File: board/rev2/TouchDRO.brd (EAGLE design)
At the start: 50.8 x 50.8 mm, 26 parts, among them U2 VREG_33, U3 VREG_5

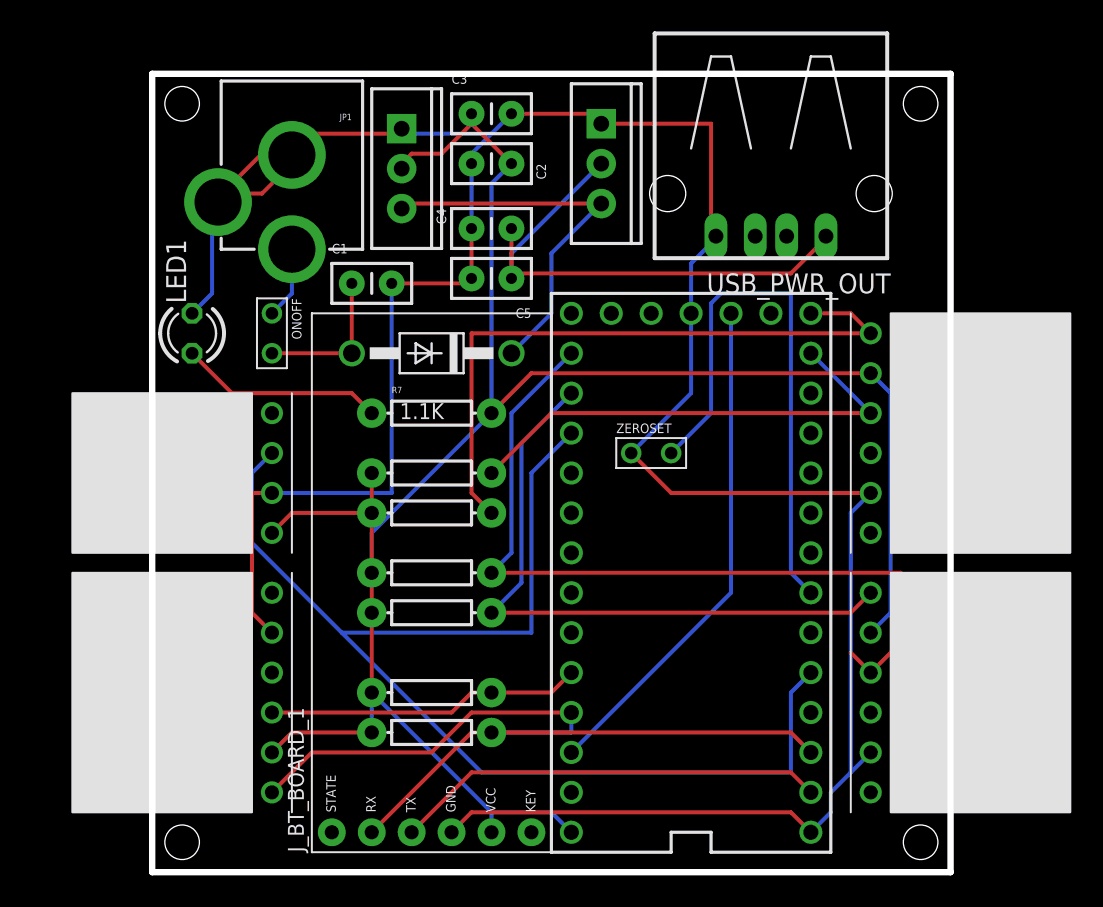
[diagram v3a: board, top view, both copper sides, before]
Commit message: move zero set connection point into reasonable location
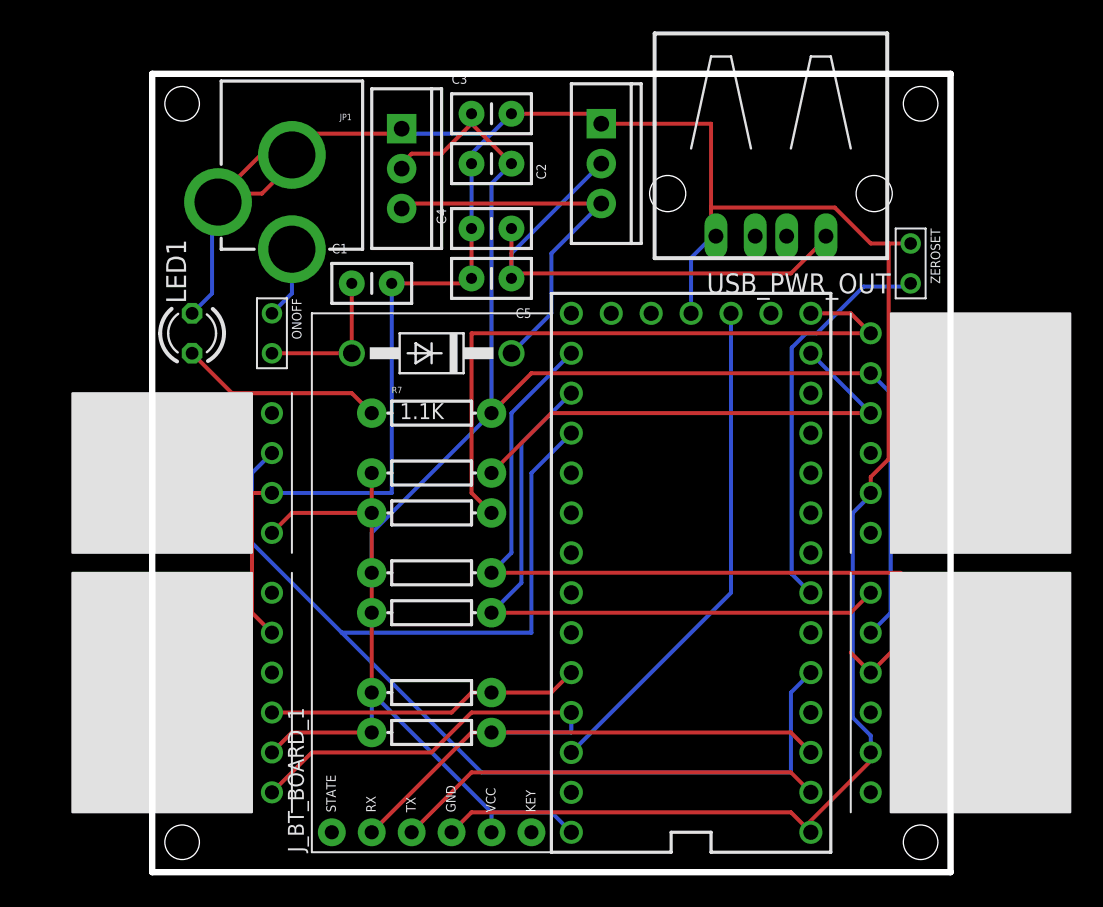
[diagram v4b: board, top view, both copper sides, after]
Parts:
- moved ZEROSET 18.7 mm to (48.3, 37.5), turned to 270 degrees
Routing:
- net ZSET: track 35.5 -> 25.5 mm
- net GND: track 183.8 -> 186.6 mm
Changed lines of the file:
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@@
 <element name="R5" library="SparkFun-Passives" package="AXIAL-0.3EZ" value="10K" x="17.78" y="11.43" smashed="yes"/>
 <element name="R6" library="SparkFun-Passives" package="AXIAL-0.3EZ" value="10K" x="17.78" y="8.89" smashed="yes"/>
-<element name="ZEROSET" library="Switches" package="DS-EXT" value="DS-227" x="33.02" y="26.67"/>
+<element name="ZEROSET" library="Switches" package="DS-EXT" value="DS-227" x="48.26" y="37.465" rot="R270"/>
 <element name="ONOFF" library="Switches" package="DS-EXT" value="DS-228" x="7.62" y="33.02" rot="R270"/>
 <element name="U2" library="regulators" package="TO220" value="VREG_33" x="15.875" y="44.7675" rot="R270"/>
@@
 <contactref element="LED1" pad="K"/>
 <contactref element="USB_PWR_OUT" pad="4"/>
-<wire x1="43.18" y1="5.08" x2="44.45" y2="6.35" width="0.254" layer="16"/>
-<wire x1="44.45" y1="6.35" x2="45.72" y2="7.62" width="0.254" layer="16"/>
-<wire x1="43.18" y1="3.81" x2="43.18" y2="5.08" width="0.254" layer="16"/>
-<wire x1="41.91" y1="2.54" x2="43.18" y2="3.81" width="0.254" layer="16"/>
-<wire x1="44.45" y1="22.86" x2="45.72" y2="24.13" width="0.254" layer="16"/>
-<wire x1="44.45" y1="6.35" x2="44.45" y2="22.86" width="0.254" layer="16"/>
 <wire x1="20.32" y1="3.81" x2="19.05" y2="2.54" width="0.254" layer="1"/>
 <wire x1="40.64" y1="3.81" x2="20.32" y2="3.81" width="0.254" layer="1"/>
@@
 <contactref element="C3" pad="2"/>
 <contactref element="C5" pad="2"/>
-<wire x1="34.29" y1="30.48" x2="30.48" y2="26.67" width="0.254" layer="16"/>
-<wire x1="34.29" y1="35.56" x2="34.29" y2="30.48" width="0.254" layer="16"/>
-<wire x1="34.29" y1="38.735" x2="35.56" y2="40.005" width="0.254" layer="16"/>
-<wire x1="34.29" y1="35.56" x2="34.29" y2="38.735" width="0.254" layer="16"/>
-<wire x1="35.56" y1="40.005" x2="35.87" y2="40.47" width="0.254" layer="16"/>
 <wire x1="6.985" y1="43.18" x2="8.89" y2="45.085" width="0.254" layer="1"/>
 <wire x1="4.445" y1="43.18" x2="6.985" y2="43.18" width="0.254" layer="1"/>
@@
 <wire x1="4.445" y1="43.18" x2="4.19" y2="42.64" width="0.254" layer="1"/>
 <wire x1="15.875" y1="46.99" x2="15.875" y2="47.3075" width="0.254" layer="1"/>
-<wire x1="35.56" y1="47.625" x2="35.56" y2="40.64" width="0.254" layer="1"/>
+<wire x1="35.56" y1="47.625" x2="35.56" y2="42.291" width="0.254" layer="1"/>
+<wire x1="35.56" y1="42.291" x2="35.56" y2="40.64" width="0.254" layer="1"/>
 <wire x1="28.575" y1="47.625" x2="35.56" y2="47.625" width="0.254" layer="1"/>
 <wire x1="35.56" y1="40.64" x2="35.87" y2="40.47" width="0.254" layer="1"/>
@@
 <wire x1="3.81" y1="42.545" x2="3.81" y2="36.83" width="0.254" layer="16"/>
 <wire x1="3.81" y1="42.545" x2="4.19" y2="42.64" width="0.254" layer="16"/>
-<wire x1="33.02" y1="24.13" x2="30.48" y2="26.67" width="0.254" layer="1"/>
-<wire x1="45.72" y1="24.13" x2="33.02" y2="24.13" width="0.254" layer="1"/>
 <wire x1="15.24" y1="24.13" x2="7.62" y2="24.13" width="0.254" layer="16"/>
 <wire x1="15.24" y1="37.465" x2="15.24" y2="24.13" width="0.254" layer="16"/>
+<wire x1="45.72" y1="7.0866" x2="45.72" y2="7.62" width="0.254" layer="1"/>
+<wire x1="41.6052" y1="2.9718" x2="45.72" y2="7.0866" width="0.254" layer="1"/>
+<wire x1="41.6052" y1="2.9718" x2="41.91" y2="2.54" width="0.254" layer="1"/>
+<wire x1="45.72" y1="40.005" x2="46.863" y2="40.005" width="0.254" layer="1"/>
+<wire x1="46.863" y1="40.005" x2="48.26" y2="40.005" width="0.254" layer="1"/>
+<wire x1="43.434" y1="42.291" x2="45.72" y2="40.005" width="0.254" layer="1"/>
+<wire x1="35.56" y1="42.291" x2="43.434" y2="42.291" width="0.254" layer="1"/>
+<wire x1="45.72" y1="25.146" x2="45.72" y2="24.13" width="0.254" layer="1"/>
+<wire x1="46.863" y1="26.289" x2="45.72" y2="25.146" width="0.254" layer="1"/>
+<wire x1="46.863" y1="40.005" x2="46.863" y2="26.289" width="0.254" layer="1"/>
+<wire x1="34.29" y1="39.0906" x2="34.29" y2="35.56" width="0.254" layer="16"/>
+<wire x1="35.6616" y1="40.4622" x2="34.29" y2="39.0906" width="0.254" layer="16"/>
+<wire x1="35.6616" y1="40.4622" x2="35.87" y2="40.47" width="0.254" layer="16"/>
+<wire x1="45.72" y1="8.6868" x2="45.72" y2="7.62" width="0.254" layer="16"/>
+<wire x1="44.577" y1="9.8298" x2="45.72" y2="8.6868" width="0.254" layer="16"/>
+<wire x1="44.577" y1="22.86" x2="44.577" y2="9.8298" width="0.254" layer="16"/>
+<wire x1="45.72" y1="24.003" x2="44.577" y2="22.86" width="0.254" layer="16"/>
+<wire x1="45.72" y1="24.003" x2="45.72" y2="24.13" width="0.254" layer="16"/>
 </signal>
 <signal name="RCV">
@@
 <contactref element="U$1" pad="5"/>
 <contactref element="ZEROSET" pad="P$2"/>
-<wire x1="35.56" y1="29.21" x2="33.02" y2="26.67" width="0.254" layer="16"/>
-<wire x1="35.56" y1="36.195" x2="35.56" y2="29.21" width="0.254" layer="16"/>
-<wire x1="36.195" y1="36.83" x2="35.56" y2="36.195" width="0.254" layer="16"/>
-<wire x1="40.64" y1="36.83" x2="36.195" y2="36.83" width="0.254" layer="16"/>
-<wire x1="40.64" y1="19.05" x2="40.64" y2="36.83" width="0.254" layer="16"/>
-<wire x1="41.91" y1="17.78" x2="40.64" y2="19.05" width="0.254" layer="16"/>
+<wire x1="45.2628" y1="37.2618" x2="48.2346" y2="37.2618" width="0.254" layer="16"/>
+<wire x1="42.291" y1="34.29" x2="45.2628" y2="37.2618" width="0.254" layer="16"/>
+<wire x1="41.6052" y1="34.29" x2="42.291" y2="34.29" width="0.254" layer="16"/>
+<wire x1="40.6908" y1="33.3756" x2="41.6052" y2="34.29" width="0.254" layer="16"/>
+<wire x1="40.6908" y1="18.9738" x2="40.6908" y2="33.3756" width="0.254" layer="16"/>
+<wire x1="41.8338" y1="17.8308" x2="40.6908" y2="18.9738" width="0.254" layer="16"/>
+<wire x1="48.2346" y1="37.2618" x2="48.26" y2="37.465" width="0.254" layer="16"/>
+<wire x1="41.8338" y1="17.8308" x2="41.91" y2="17.78" width="0.254" layer="16"/>
 </signal>
 <signal name="N$1">

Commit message: added bluetooth KEY signal. changed pins in microcontroller code to match new design
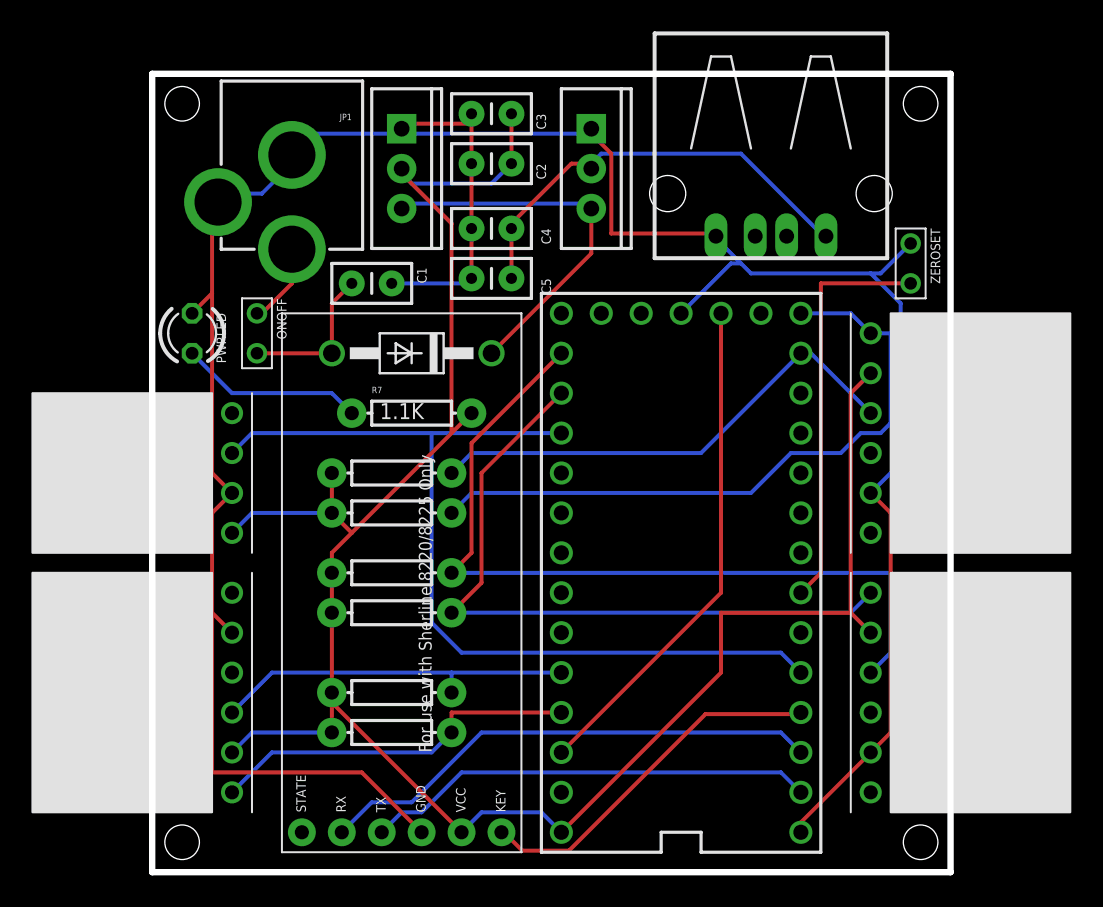
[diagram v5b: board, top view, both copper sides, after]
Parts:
- moved R1 2.54 mm to (15.2, 25.4)
- moved R2 2.54 mm to (15.2, 22.9)
- moved R3 2.54 mm to (15.2, 19.1)
- moved R4 2.54 mm to (15.2, 16.5)
- moved R5 2.54 mm to (15.2, 11.4)
- moved R6 2.54 mm to (15.2, 8.89)
- moved TACH 2.54 mm to (5.08, 21.6)
- moved Z_AXIS 2.54 mm to (-1.27, 8.89)
- moved C3 2.54 mm to (22.9, 48.3), turned to 180 degrees
- moved J_BT_BOARD_1 1.91 mm to (15.9, 19.1)
- moved D3 1.27 mm to (16.5, 33.0)
- moved R7 1.27 mm to (16.5, 29.2)
- moved ONOFF 0.95 mm to (6.67, 33.0)
- moved U3 0.71 mm to (27.9, 44.8)
- moved U$1 0.63 mm to (33.7, 19.1)
- renumbered LED1 to PWRLED
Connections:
- new net KEY: J_BT_BOARD_1.KEY, U$1.2
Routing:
- net KEY: track 0.00 -> 23.2 mm
- net T: track 79.3 -> 58.4 mm
- net GND: track 186.6 -> 176.7 mm
- net +5V: track 33.9 -> 28.1 mm
- net +3V3: track 130.4 -> 134.6 mm
- net Z_B: track 27.5 -> 23.8 mm
- net Y_B: track 40.7 -> 44.1 mm
- net Z_A: track 20.1 -> 23.3 mm
- net RCV: track 27.5 -> 28.8 mm
- net N$1: track 13.0 -> 11.7 mm
- net TR: track 31.1 -> 32.4 mm
- net Y_A: track 51.0 -> 51.7 mm
- net N$6: track 4.61 -> 5.19 mm
- net X_B: track 41.7 -> 42.3 mm

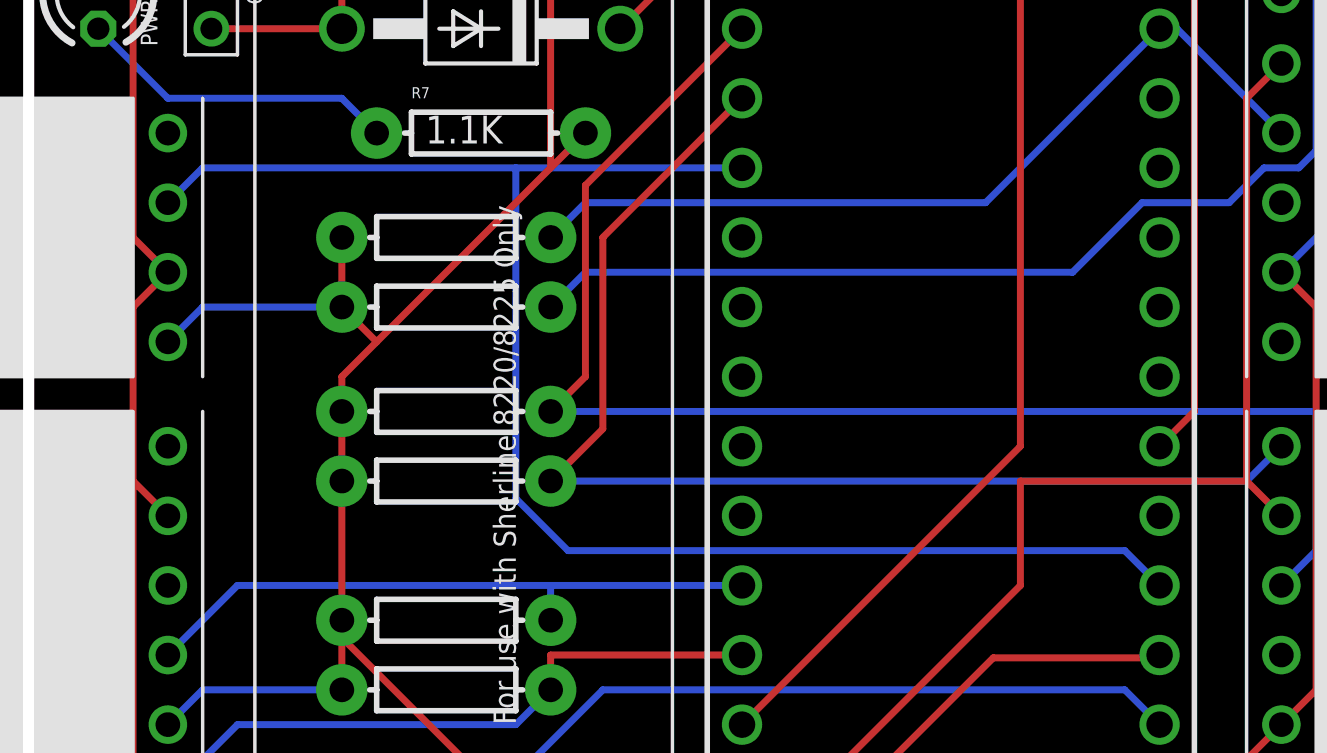
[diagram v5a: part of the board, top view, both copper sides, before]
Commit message: modified rev2 board to use multifrequencymeasure library (which allows to specify of pin)
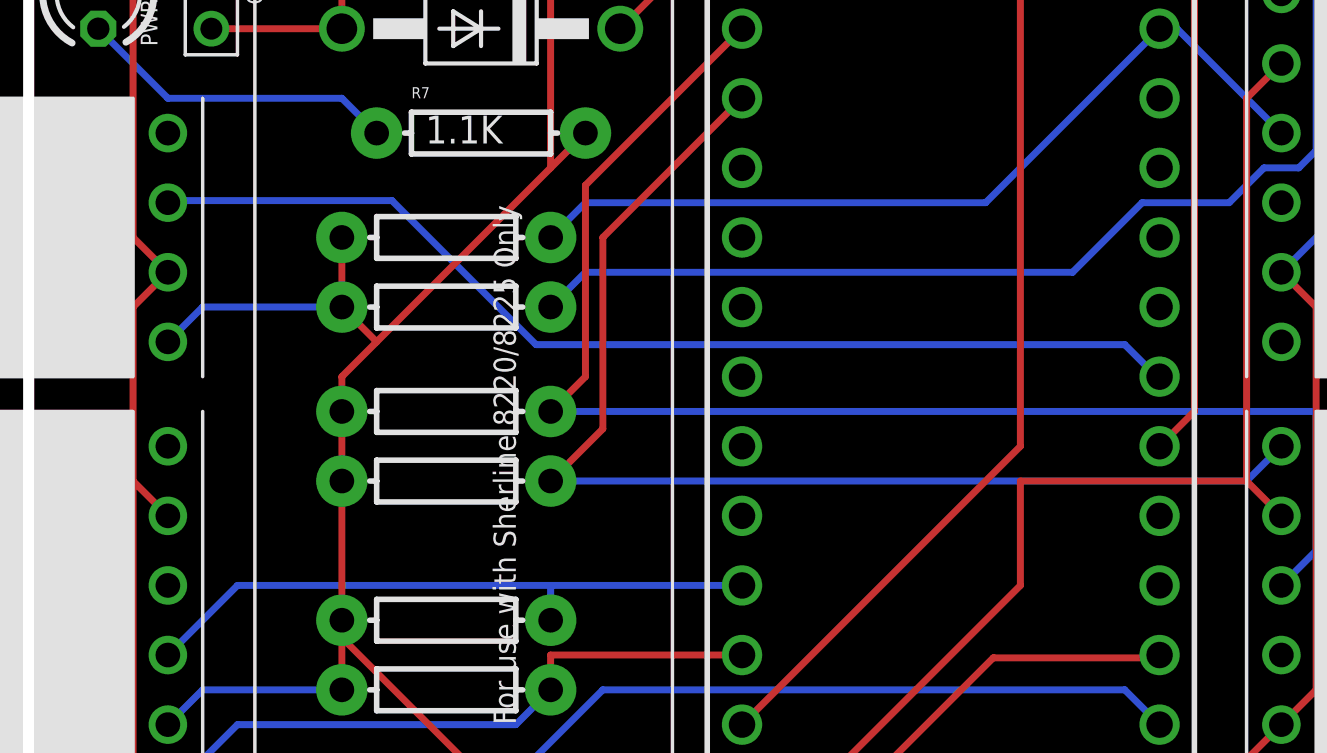
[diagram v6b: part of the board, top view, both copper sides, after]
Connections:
- net T: now also U$1.6; no longer U$1.16/A2, U$1.3
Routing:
- net T: track 58.4 -> 38.9 mm
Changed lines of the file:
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@@
 <signal name="T">
 <contactref element="TACH" pad="P$3"/>
-<contactref element="U$1" pad="3"/>
-<contactref element="U$1" pad="16/A2"/>
-<wire x1="6.35" y1="27.94" x2="5.08" y2="26.67" width="0.254" layer="16"/>
-<wire x1="26.035" y1="27.94" x2="17.78" y2="27.94" width="0.254" layer="16"/>
-<wire x1="17.78" y1="27.94" x2="6.35" y2="27.94" width="0.254" layer="16"/>
-<wire x1="40.005" y1="13.97" x2="41.275" y2="12.7" width="0.254" layer="16"/>
-<wire x1="19.685" y1="13.97" x2="40.005" y2="13.97" width="0.254" layer="16"/>
-<wire x1="17.78" y1="15.875" x2="19.685" y2="13.97" width="0.254" layer="16"/>
-<wire x1="17.78" y1="27.94" x2="17.78" y2="15.875" width="0.254" layer="16"/>
+<contactref element="U$1" pad="6"/>
+<wire x1="13.2588" y1="26.7462" x2="5.2578" y2="26.7462" width="0.254" layer="16"/>
+<wire x1="18.5166" y1="21.4884" x2="13.2588" y2="26.7462" width="0.254" layer="16"/>
+<wire x1="40.005" y1="21.4884" x2="18.5166" y2="21.4884" width="0.254" layer="16"/>
+<wire x1="41.148" y1="20.3454" x2="40.005" y2="21.4884" width="0.254" layer="16"/>
+<wire x1="5.2578" y1="26.7462" x2="5.08" y2="26.67" width="0.254" layer="16"/>
+<wire x1="41.148" y1="20.3454" x2="41.275" y2="20.32" width="0.254" layer="16"/>
 </signal>
 <signal name="N$6">
